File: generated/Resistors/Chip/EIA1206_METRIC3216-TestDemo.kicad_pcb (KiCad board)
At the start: 2 copper layers, 1 part

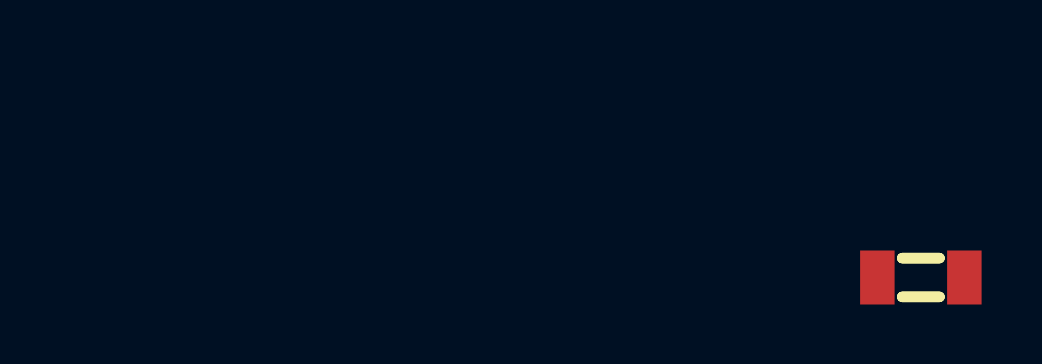
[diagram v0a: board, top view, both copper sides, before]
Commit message: add Chip EIA 1206 resistors
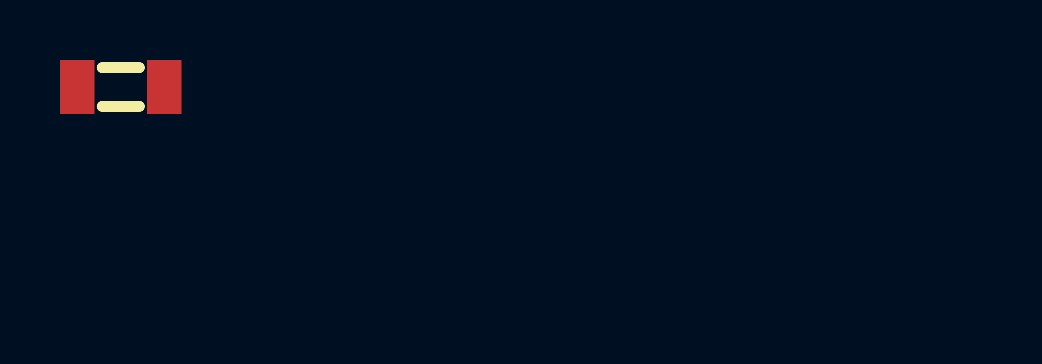
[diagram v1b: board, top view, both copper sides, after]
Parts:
- moved REF** 27.4 mm to (25.4, 25.4)
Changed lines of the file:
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@@
   )
   (module RESC3216X65 (layer F.Cu)
-    (at 52.07 31.75)
+    (at 25.4 25.4)
     (descr "Resistor,Chip;3.20mm L X 1.60mm W X 0.65mm H")
     (attr smd)
@@
     (pad 2 smd rect (at 1.45 0) (size 1.15 1.8) (layers F.Cu F.Paste F.Mask))
     (pad 1 smd rect (at -1.45 0) (size 1.15 1.8) (layers F.Cu F.Paste F.Mask))
-    (model ${KIPRJMOD}/RESC3216x66_EIA1206_METRIC3216.wrl
+    (model ${KIPRJMOD}/EIA1206_METRIC3216/000.wrl
       (at (xyz 0 0 0))
       (scale (xyz 1 1 1))
